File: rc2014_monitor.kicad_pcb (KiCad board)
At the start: 2 copper layers, 99.1 x 49.9 mm, 28 parts, among them J1 RC2014Pro, J3 USB_B_Micro, SW1 SW_Coded_Octal-8, U1 74HCT138, U2 74HCT151, U3 74HCT244, U4 74HCT244, U5 74HCT244, U6 74HCT32

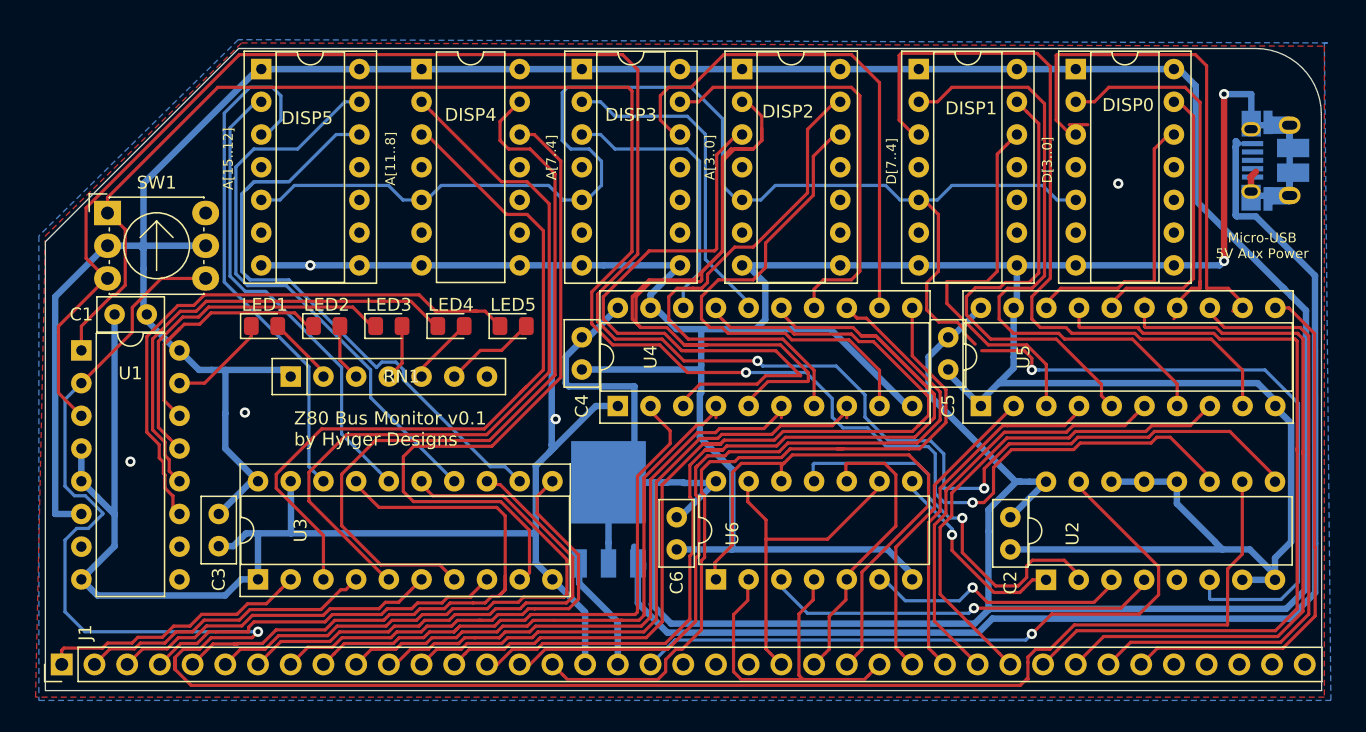
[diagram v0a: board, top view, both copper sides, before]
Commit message: replaces schottky with ideal diodes
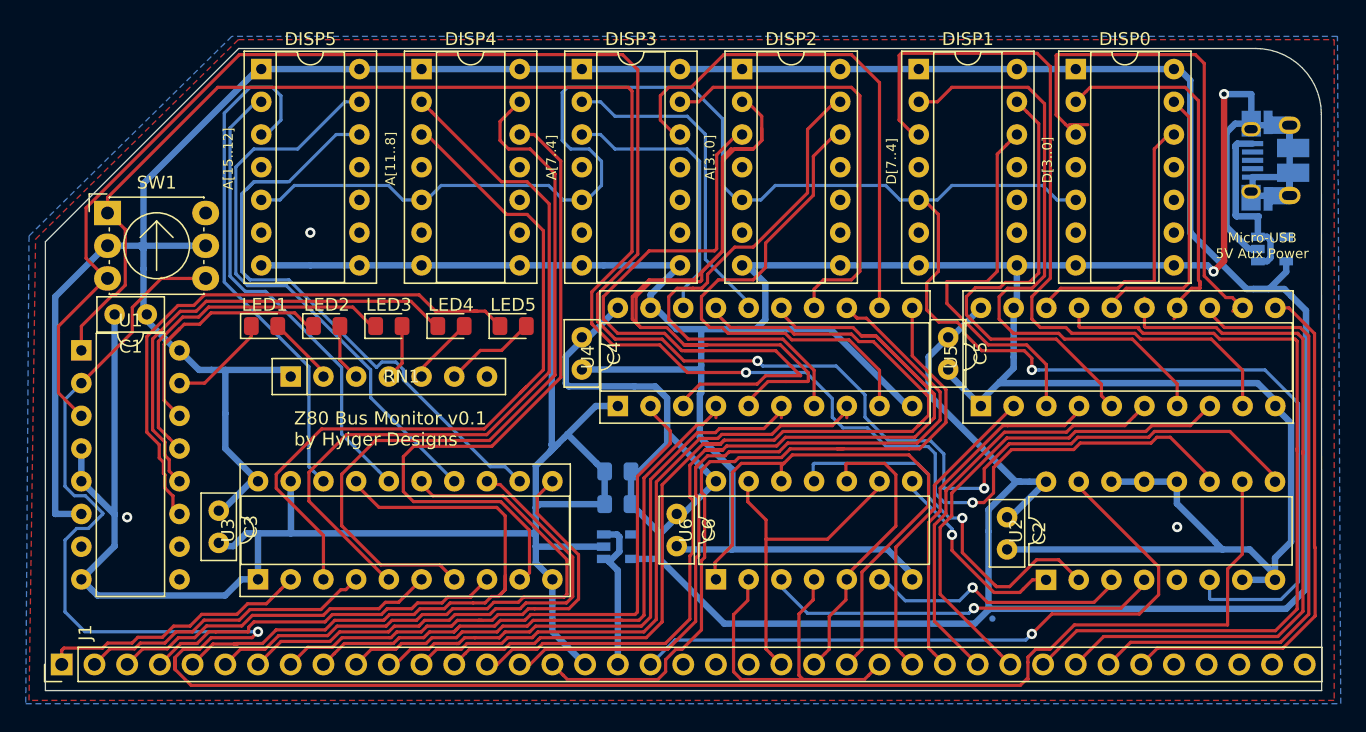
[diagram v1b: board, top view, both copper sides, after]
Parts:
- removed D1: Schottky Diodes & Rectifiers 40V Vr; 6A, Package_TO_SOT_SMD:TO-252-3_TabPin2
- added C7: 100nF, Capacitor_SMD:C_0805_2012Metric_Pad1.15x1.40mm_HandSolder, B.Cu at (120.7, 110.2)
- added C8: 1uF, Capacitor_SMD:C_0805_2012Metric_Pad1.15x1.40mm_HandSolder, B.Cu at (120.7, 112.8)
- added U7: MAX40200AUK, Package_TO_SOT_SMD:SOT-23-5, B.Cu at (171.4, 93.0)
- added U8: MAX40200AUK, Package_TO_SOT_SMD:SOT-23-5, B.Cu at (120.7, 116.1)
- DISP4: footprint Package_DIP:DIP-14_W7.62mm -> Package_DIP:DIP-14_W7.62mm_Socket
- moved C6 0.25 mm to (125.2, 113.5)
- moved C2 0.25 mm to (150.9, 113.8)
- moved C3 0.25 mm to (89.7, 113.3)
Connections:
- DISP0 pad 10: Net-(DISP0-Pad10) -> (no net)
- DISP0 pad 4: Net-(DISP0-Pad4) -> (no net)
- DISP1 pad 10: Net-(DISP1-Pad10) -> (no net)
- DISP1 pad 4: Net-(DISP1-Pad4) -> (no net)
- DISP2 pad 10: Net-(DISP2-Pad10) -> (no net)
- DISP2 pad 4: Net-(DISP2-Pad4) -> (no net)
- DISP3 pad 10: Net-(DISP3-Pad10) -> (no net)
- DISP3 pad 4: Net-(DISP3-Pad4) -> (no net)
- DISP4 pad 10: Net-(DISP4-Pad10) -> (no net)
- DISP4 pad 4: Net-(DISP4-Pad4) -> (no net)
- DISP5 pad 10: Net-(DISP5-Pad10) -> (no net)
- DISP5 pad 4: Net-(DISP5-Pad4) -> (no net)
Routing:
- net Net-(J3-Pad1): track 105.7 -> 19.3 mm
- net GND: track 393.9 -> 427.6 mm, vias 7 -> 5
- net +5V: track 344.2 -> 339.4 mm
- net 5V: track 10.3 -> 12.3 mm
- net D_D3: track 41.5 -> 40.6 mm
- net LATCH: track 151.5 -> 152.2 mm
- net D_D1: track 21.7 -> 21.2 mm

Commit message: added additional LED for 5V signal
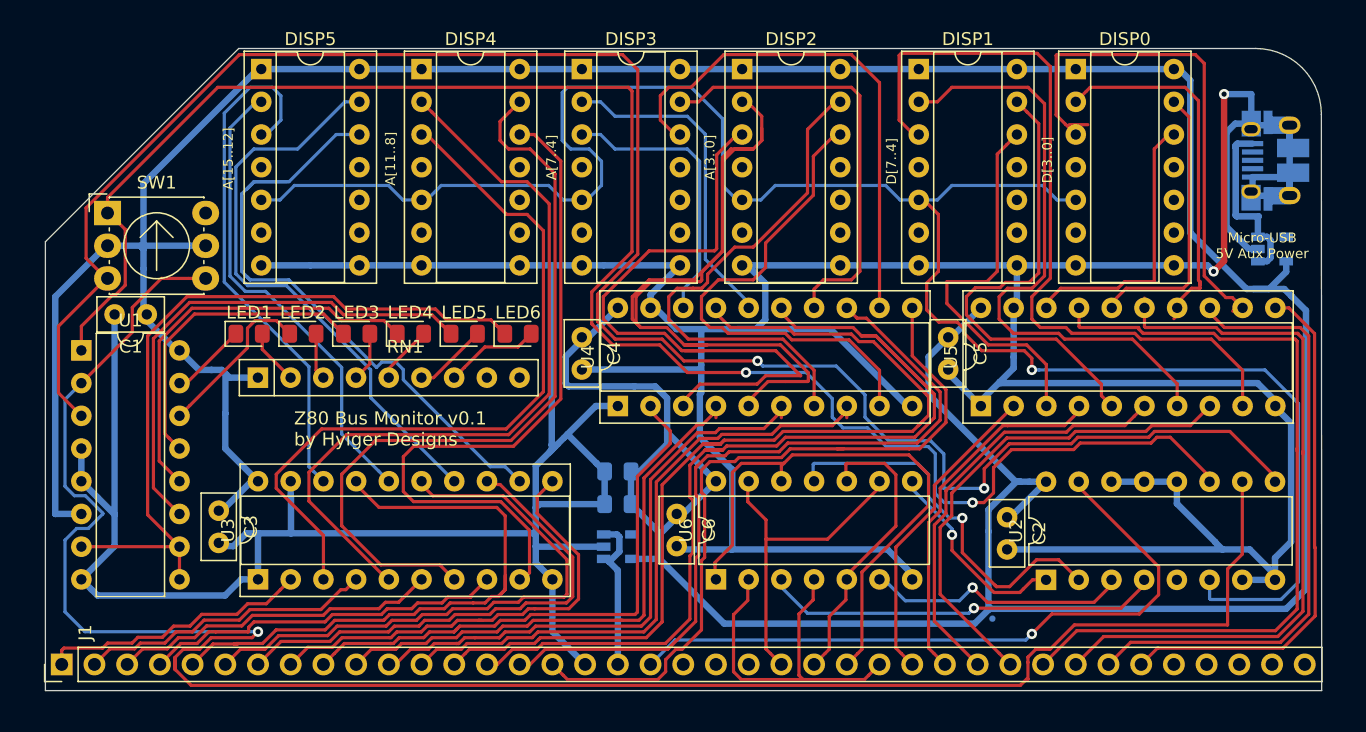
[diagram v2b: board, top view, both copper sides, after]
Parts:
- added LED6: SMD Red 620nm 40mcd 2.2V; 20mA, LED_SMD:LED_0805_2012Metric_Pad1.15x1.40mm_HandSolder, F.Cu at (112.9, 99.5)
- RN1: value R_Network06 -> 270R Bussed; footprint Resistor_THT:R_Array_SIP7 -> Resistor_THT:R_Array_SIP9
- moved LED5 3.85 mm to (108.7, 99.5)
- moved LED4 3.21 mm to (104.5, 99.5)
- moved LED3 2.57 mm to (100.4, 99.5)
- moved RN1 2.55 mm to (92.7, 103.0)
- moved LED2 1.94 mm to (96.2, 99.5)
- moved LED1 1.34 mm to (92.0, 99.5)
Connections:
- RN1 pad 7: (no net) -> Net-(LED6-Pad2)
- U1 pad 10: (no net) -> Net-(LED6-Pad1)
- U1 pad 7: (no net) -> Net-(LED6-Pad1)
- U1 pad 9: (no net) -> Net-(LED6-Pad1)
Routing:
- net Net-(LED6-Pad1): track 0.00 -> 57.7 mm
- net Net-(LED6-Pad2): track 0.00 -> 7.40 mm
- net Net-(LED2-Pad1): track 20.2 -> 12.9 mm
- net Net-(LED5-Pad1): track 44.9 -> 40.5 mm
- net Net-(LED4-Pad1): track 35.9 -> 31.9 mm
- net Net-(LED3-Pad1): track 27.3 -> 24.1 mm
- net +5V: track 339.4 -> 336.8 mm
- net Net-(LED1-Pad1): track 7.88 -> 5.97 mm
- net Net-(LED1-Pad2): track 5.39 -> 4.32 mm
- net D_A10: track 59.1 -> 60.1 mm
- net D_A9: track 58.8 -> 59.8 mm
- net D_A8: track 53.7 -> 54.7 mm
- net Net-(LED5-Pad2): track 7.19 -> 6.37 mm
- net Net-(LED4-Pad2): track 5.29 -> 4.53 mm
- net Net-(LED2-Pad2): track 4.69 -> 4.01 mm
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- removed copper zone on B.Cu, net GND
- removed copper zone on F.Cu, net GND

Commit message: Added mounting hole
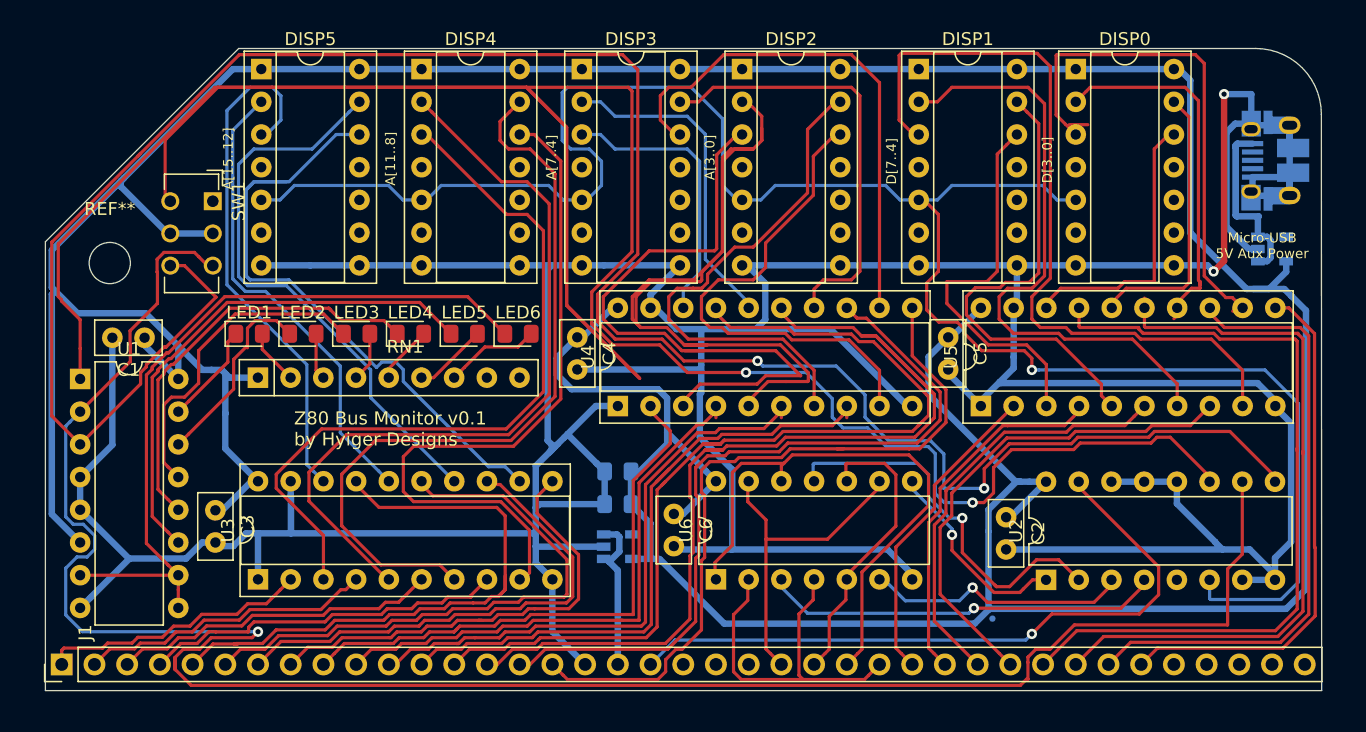
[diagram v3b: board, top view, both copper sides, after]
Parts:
- added REF**: MountingHole_3.2mm_M3, MountingHole:MountingHole_3.2mm_M3, F.Cu at (81.2, 94.1)
- SW1: footprint Button_Switch_THT:Nidec_Copal_SH-7010C -> Button_Switch_THT:SW_Greyhill_94HBB08RAT_Octal_Angled
- moved SW1 8.23 mm to (89.2, 89.3), turned to 270 degrees
- moved U1 2.22 mm to (78.9, 103.1)
- moved C1 1.82 mm to (83.9, 99.9)
- moved C4 0.36 mm to (117.5, 99.8)
- moved C3 0.26 mm to (89.4, 113.3)
- moved C6 0.22 mm to (125.0, 113.5)
- moved C2 0.08 mm to (150.8, 113.8)
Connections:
- SW1 pad 8: (no net) -> Net-(SW1-Pad8)
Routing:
- net Net-(SW1-Pad1): track 139.1 -> 228.5 mm
- net Net-(SW1-Pad4): track 153.4 -> 175.6 mm
- net +5V: track 336.8 -> 350.2 mm
- net GND: track 427.6 -> 417.7 mm
- net Net-(LED2-Pad1): track 12.9 -> 15.4 mm
- net Net-(LED1-Pad1): track 5.97 -> 7.90 mm
- net Net-(LED4-Pad1): track 31.9 -> 33.5 mm
- net Net-(SW1-Pad2): track 158.4 -> 159.8 mm
- net A4: track 48.2 -> 49.6 mm
- net Net-(LED3-Pad1): track 24.1 -> 25.1 mm
- net Net-(LED6-Pad1): track 57.7 -> 58.4 mm

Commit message: moved latch circuit to new sheet
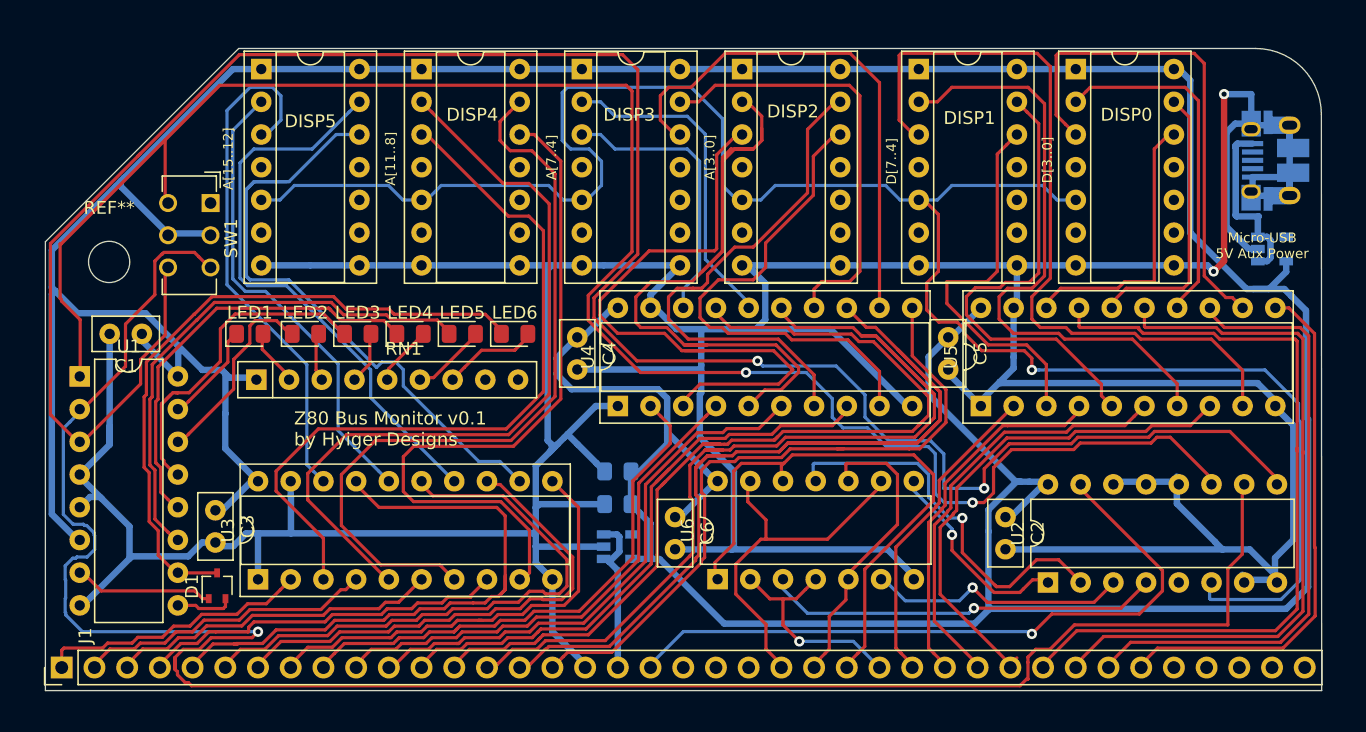
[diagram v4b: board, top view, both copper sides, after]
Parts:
- added D1: BAT54AW, Package_TO_SOT_SMD:SOT-323_SC-70, F.Cu at (89.5, 119.1)
- moved SW1 3.05 mm to (87.8, 91.9), turned to 0 degrees
- moved C1 0.36 mm to (83.7, 99.6)
- moved LED6 0.26 mm to (112.6, 99.6)
- moved C6 0.26 mm to (125.1, 113.8)
- moved U2 0.25 mm to (154.1, 118.9)
- moved J1 0.24 mm to (77.5, 125.5)
- moved U1 0.20 mm to (78.9, 102.9)
- moved LED2 0.20 mm to (96.4, 99.6)
- moved RN1 0.20 mm to (92.6, 103.1)
- moved LED5 0.15 mm to (108.6, 99.6)
- moved U6 0.13 mm to (128.4, 118.6)
- moved REF** 0.10 mm to (81.2, 94.0)
- moved LED3 0.09 mm to (100.5, 99.6)
- moved LED1 0.06 mm to (92.1, 99.6)
- moved C2 0.05 mm to (150.7, 113.8)
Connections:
- LED6 pad 1: Net-(LED6-Pad1) -> Net-(D1-Pad3)
- RN1 pad 8: (no net) -> Net-(RN1-Pad8)
- RN1 pad 9: (no net) -> Net-(RN1-Pad9)
- U1 pad 10: Net-(LED6-Pad1) -> Net-(D1-Pad3)
- U1 pad 7: Net-(LED6-Pad1) -> Net-(D1-Pad1)
- U1 pad 9: Net-(LED6-Pad1) -> Net-(D1-Pad2)
- U2 pad 5: (no net) -> Net-(U2-Pad5)
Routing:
- net Net-(SW1-Pad1): track 228.5 -> 146.5 mm
- net Net-(LED6-Pad1): track 58.4 -> 0.00 mm
- net Net-(D1-Pad3): track 0.00 -> 51.7 mm
- net A1: track 60.0 -> 82.4 mm
- net D_A2: track 70.6 -> 59.5 mm
- net ~IORQ: track 28.0 -> 17.2 mm, vias 0 -> 1
- net Net-(D1-Pad1): track 0.00 -> 10.6 mm
- net A0: track 57.8 -> 53.3 mm
- net Net-(D1-Pad2): track 0.00 -> 4.21 mm
- net Net-(SW1-Pad4): track 175.6 -> 171.7 mm
- net A6: track 43.6 -> 39.7 mm
- net A5: track 45.9 -> 42.5 mm
- net A4: track 49.6 -> 46.4 mm
- net A2: track 75.4 -> 72.5 mm
- net A3: track 76.0 -> 73.1 mm
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
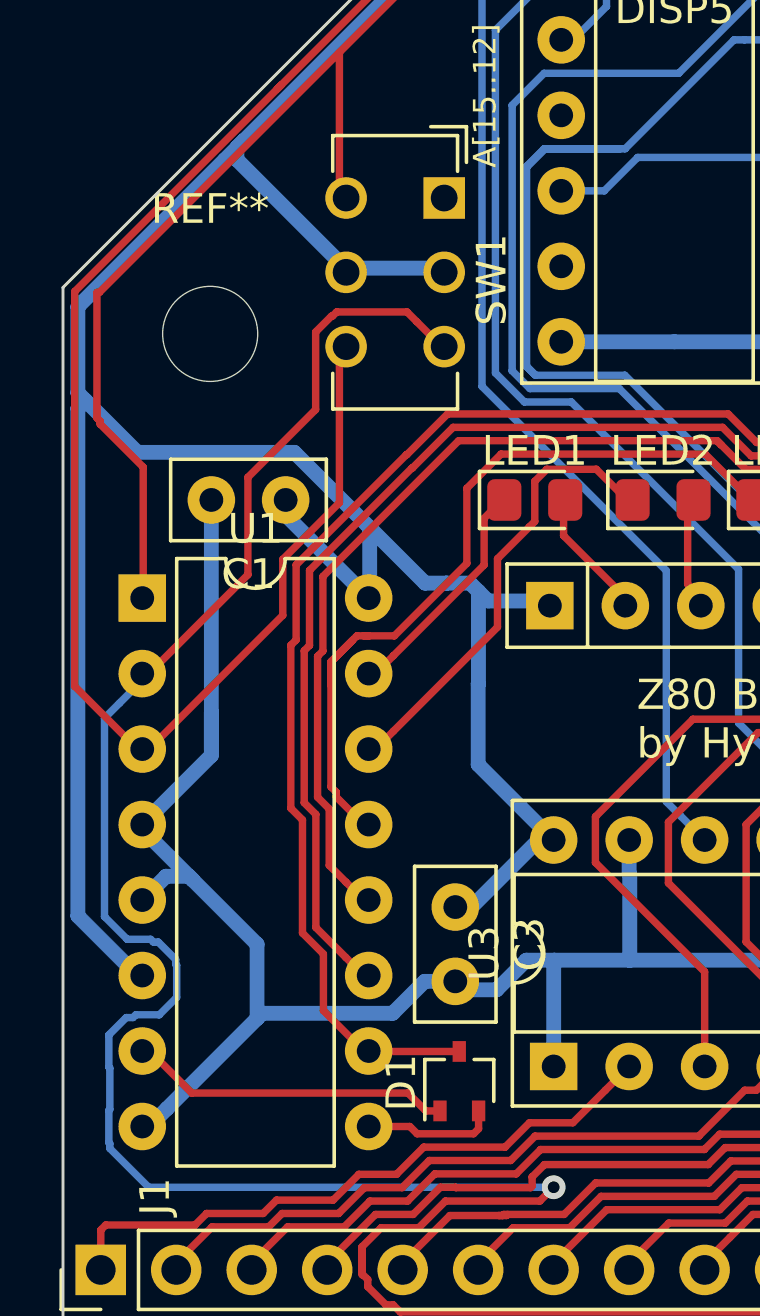
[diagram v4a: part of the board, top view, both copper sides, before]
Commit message: added diode-AND to unused latch select pins
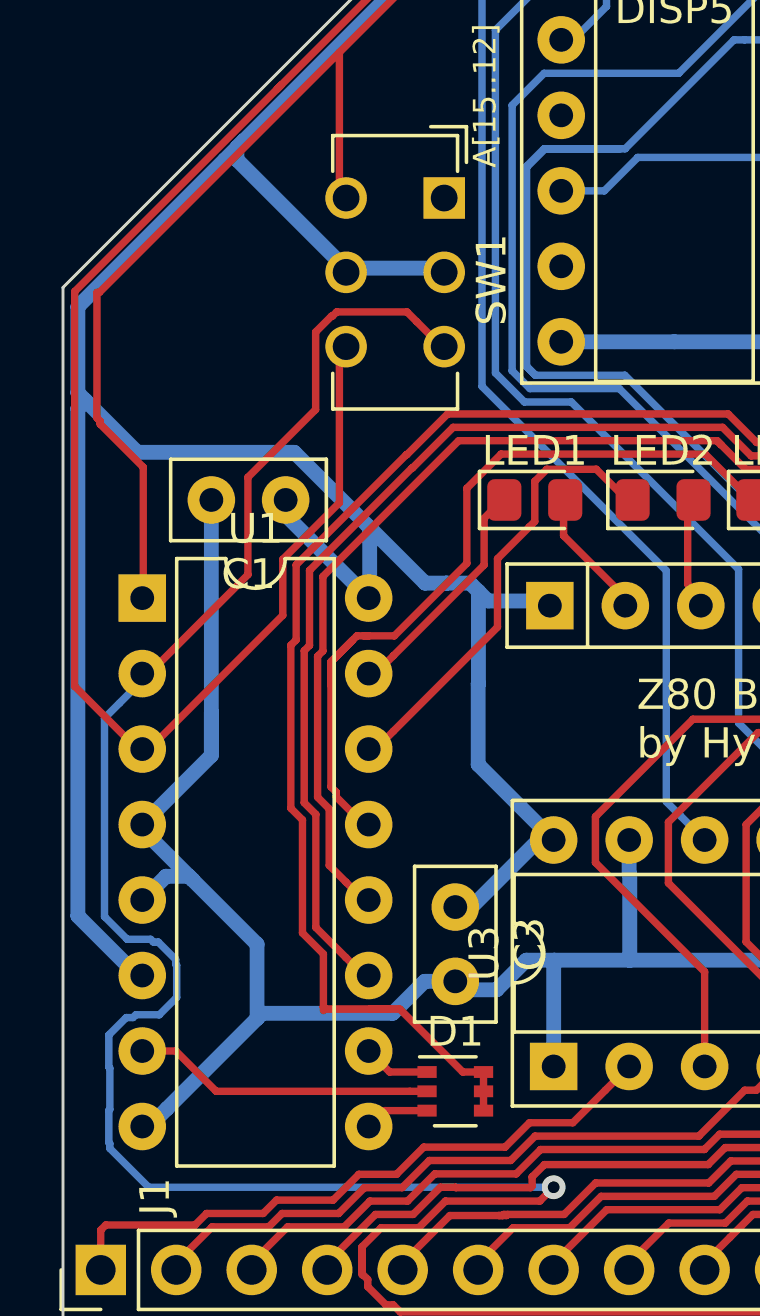
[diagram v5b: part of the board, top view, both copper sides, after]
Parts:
- removed REF**: MountingHole_3.2mm_M3, MountingHole:MountingHole_3.2mm_M3
- D1: value BAT54AW -> SD103ATW; footprint Package_TO_SOT_SMD:SOT-323_SC-70 -> Package_TO_SOT_SMD:SOT-363_SC-70-6
- moved D1 0.37 mm to (89.4, 119.5), turned to 0 degrees
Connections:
- LED6 pad 1: Net-(D1-Pad3) -> Net-(D1-Pad4)
- RN1 pad 8: Net-(RN1-Pad8) -> (no net)
- RN1 pad 9: Net-(RN1-Pad9) -> (no net)
- SW1 pad 8: Net-(SW1-Pad8) -> (no net)
- U1 pad 10: Net-(D1-Pad3) -> Net-(D1-Pad1)
- U1 pad 7: Net-(D1-Pad1) -> Net-(D1-Pad2)
- U1 pad 9: Net-(D1-Pad2) -> Net-(D1-Pad3)
- U2 pad 5: Net-(U2-Pad5) -> (no net)
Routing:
- net Net-(D1-Pad4): track 0.00 -> 54.9 mm
- net Net-(D1-Pad3): track 51.7 -> 2.19 mm
- net Net-(D1-Pad1): track 10.6 -> 2.28 mm
- net Net-(D1-Pad2): track 4.21 -> 10.1 mm
